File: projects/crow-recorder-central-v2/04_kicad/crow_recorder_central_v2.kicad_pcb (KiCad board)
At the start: 6 copper layers, 170 x 120 mm, 198 parts, among them J1 C381116, J10 C9900035627, J2 C3020560, J3 C9900035627, J4 C9900035627, J5 C9900035627, J6 C9900035627, J7 C9900035627, J8 C9900035627, J9 C9900035627, Q1 C15127, Q2 C20917, U1 C6938291, U10 C6035451, U2 C181312, U3 C181312, U4 C232798, U5 C82317, U6 C2909890, U7 C5224055, U8 C5224055, U9 C150173, Y1 C7190380

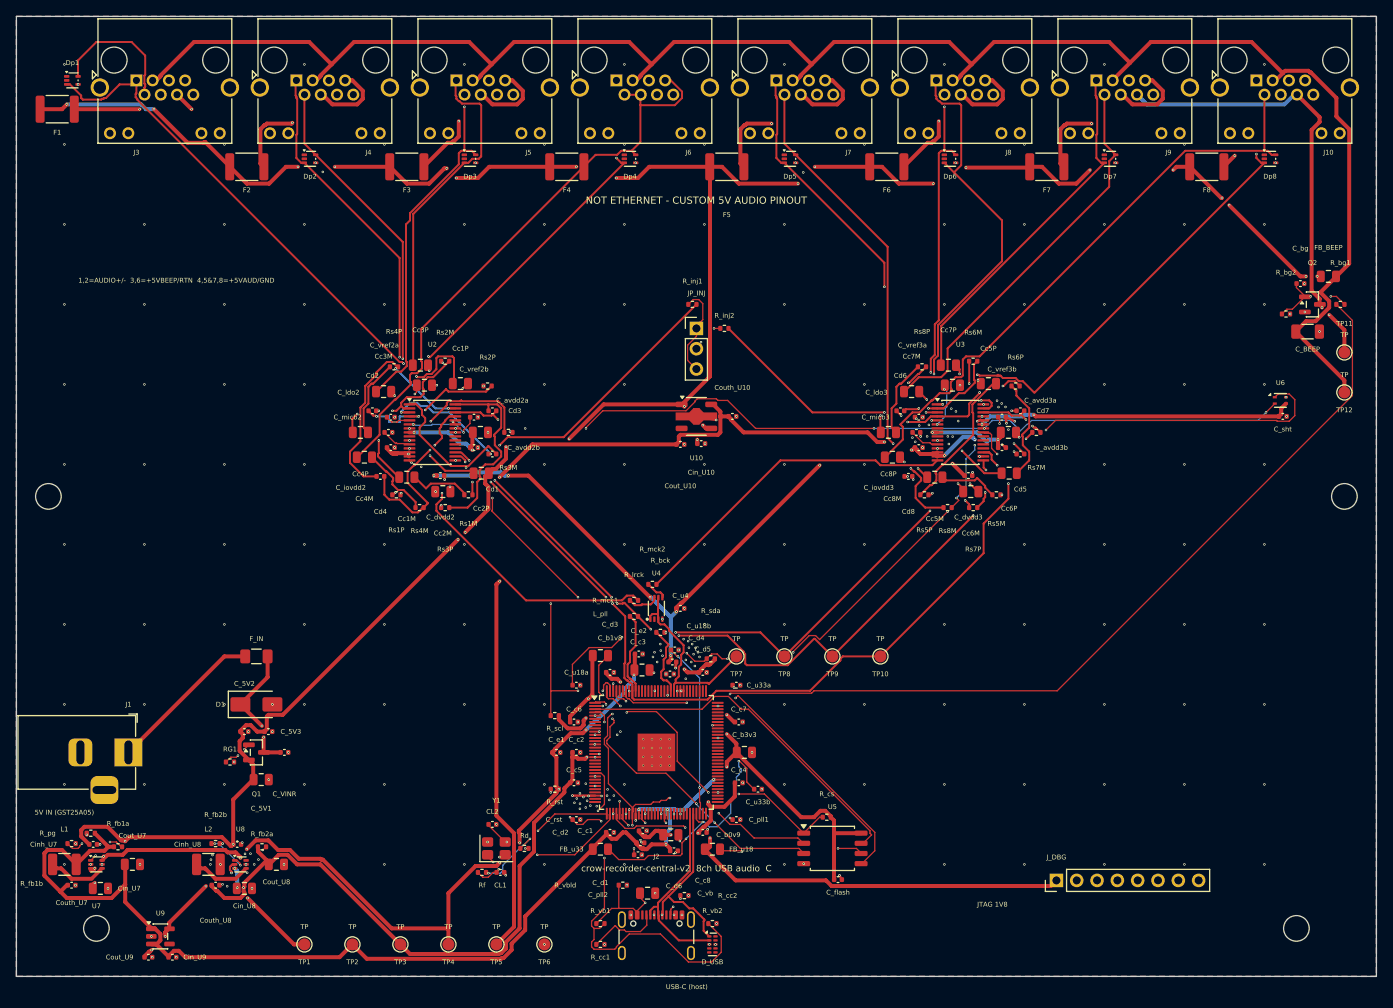
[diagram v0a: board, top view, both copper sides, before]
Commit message: crow-recorder-central-v2 WIP checkpoint: mid-P0 fix pass at the 2026-07-23 quota stop
Session-quota interruption checkpoint. Carries the interrupted P5VA_4
net-merge surgery (schematic doglegs, merged-net tree deletion, port-4 +
channel-2 re-route, 5V island reconnection), check_port_nets.py (the
label-survival gate that found the SECOND merge MID2P->5V the red-team
missed), ADR-0007 PoE-backfeed draft, rebuild_reuse.sh driver, BLM21
part. NOT a green gate — DRC re-verify + scoped re-red-team still owed
(RESUME.md is the brief). GUARD from the red-team dispositions: Q1
reverse-polarity is CORRECT as-built (rejected finding — do not "fix").

Co-Authored-By: Claude Fable 5 <noreply@anthropic.com>
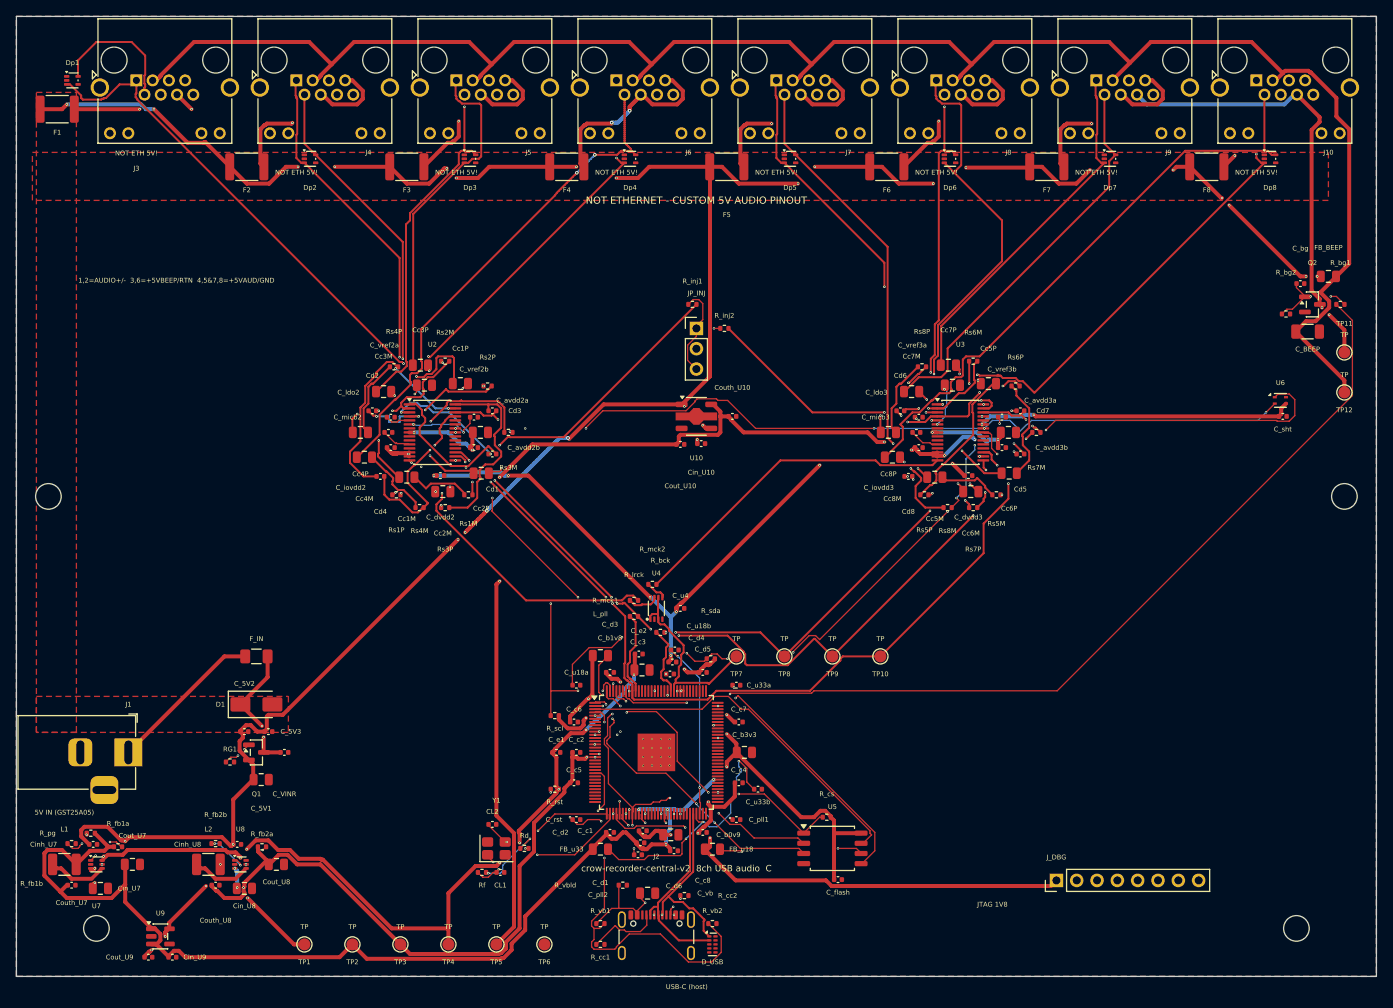
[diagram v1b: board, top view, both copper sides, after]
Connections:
- Cc2P pad 2: 5V -> MID2P
- F4 pad 2: AUDIO4M -> P5VA_4
- J6 pad 4: AUDIO4M -> P5VA_4
- J6 pad 7: AUDIO4M -> P5VA_4
- Rs2P pad 1: 5V -> MID2P
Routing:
- net P5VA_4: track 0.00 -> 24.1 mm, vias 0 -> 2
- net GND: track 21.2 -> 0.00 mm, vias 311 -> 0
- net MID2P: track 0.00 -> 13.3 mm, vias 0 -> 2
- net 5V: track 370.6 -> 358.0 mm, vias 34 -> 33
- net AUDIO4M: track 74.7 -> 63.6 mm, vias 0 -> 2
- added copper zone on F.Cu, net 5V
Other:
- board text added: "NOT ETH 5V!"

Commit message: crow-recorder-central-v2: P0 fix RE-VERIFIED from committed source; P1 set closed; policy_audit 0 FAIL
Resumed from WIP 8017400 (killed mid-rebuild = untrustworthy; re-ran
rebuild_reuse.sh clean). Measured: check_port_nets 115/115 labels + 8/8
ports pin-for-pin; DRC 0/0/0 (--severity-all --refill-zones
--schematic-parity); E-INV 7/7; E-TOPO 2/2; count_parity 194 x4.

route.yaml: unify_zone_priorities dropped from the stitch pass list — the
pass hard-refuses cross-net zone-outline overlap, but the deliberate 5V
patch-pours over the board-wide F.Cu GND pour are priority-resolved and
DRC-gated; usb-hub-3s-v3 sealed with the same pattern and the same pass
absent.

P1 closure (measured evidence in journal + DISPOSITIONS.md): 5V trunk 159
segs all 0.5mm + 1144mm2 pour patches, 6 netclasses in the final
.kicad_pro; P-ADJ over-spans re-measured at their local subjects and
waived with numbers; 8x per-port NOT-ETH silk verified on the board;
ADR-0007 finalized carrying the pod-v2 ADR-0005 USER waiver with an
explicit material-difference check (equal-or-lesser exposure here).

NEW GATE 03_src/audit_board.py (P-POL/P-KEEP): 19 polarity facts + 11
connector keepout checks; red-tested (swapped D1 fact -> FAIL, nonzero).
Waivers: S-OCCL (converter sheet is the machine artifact), P-ADJ (per-net
measurements), R-THERM (U1 EP served by 16 footprint-embedded 0.3mm PTH
thermal pads — checker counts only PCB_VIA objects). 08_reviews/
populated: reconstructed red-team review (verbatim lost to the quota
kill — provenance note in-file) + dispositions ledger.

Co-Authored-By: Claude Fable 5 <noreply@anthropic.com>
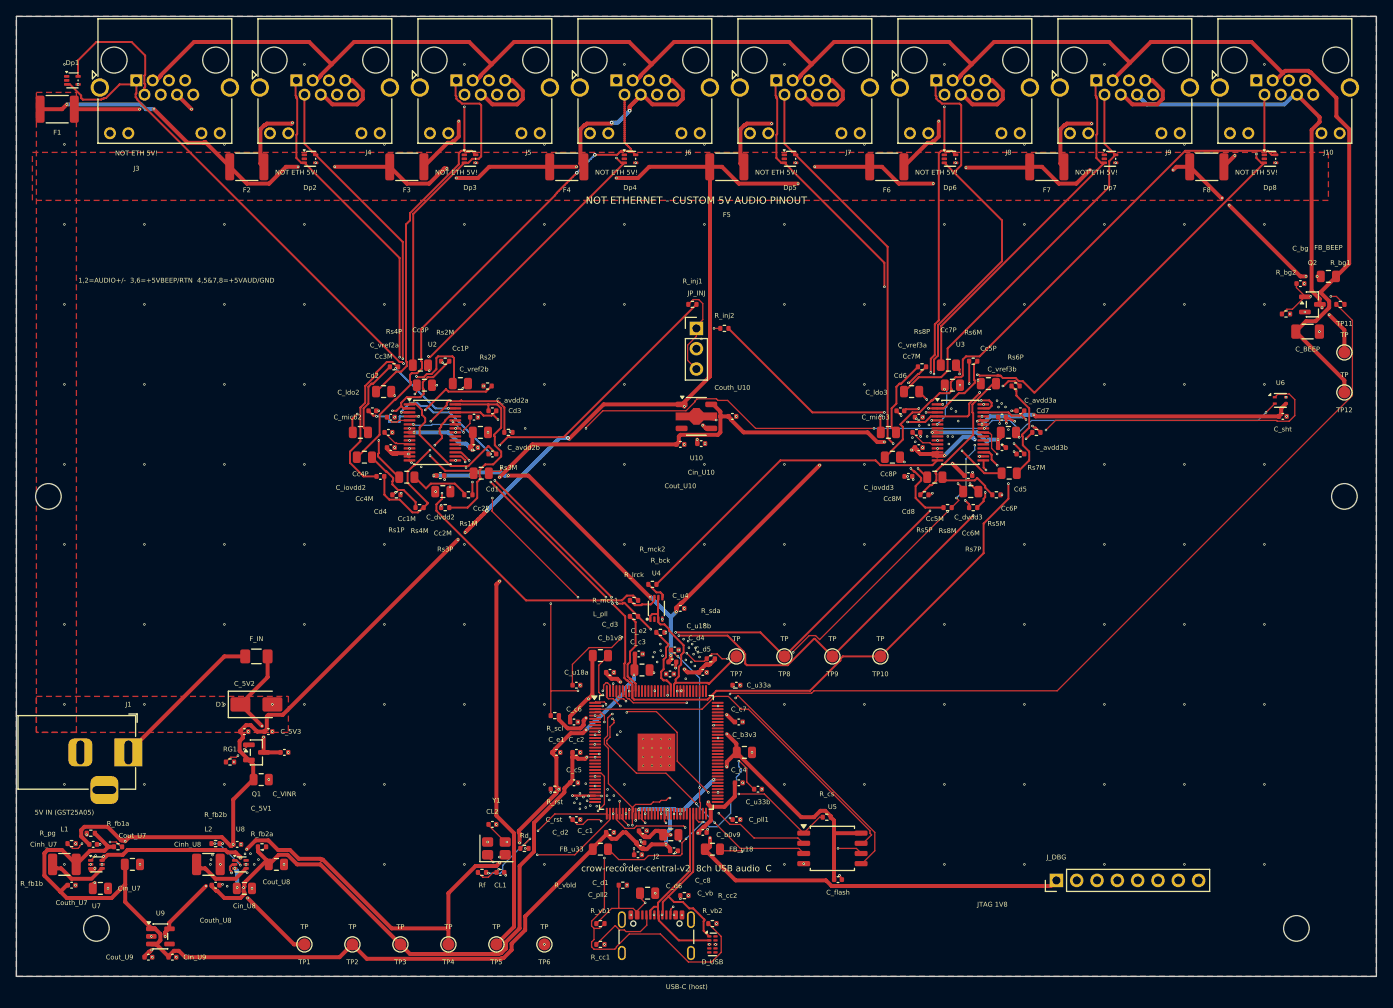
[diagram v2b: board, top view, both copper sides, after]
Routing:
- net GND: track 0.00 -> 21.2 mm, vias 0 -> 307

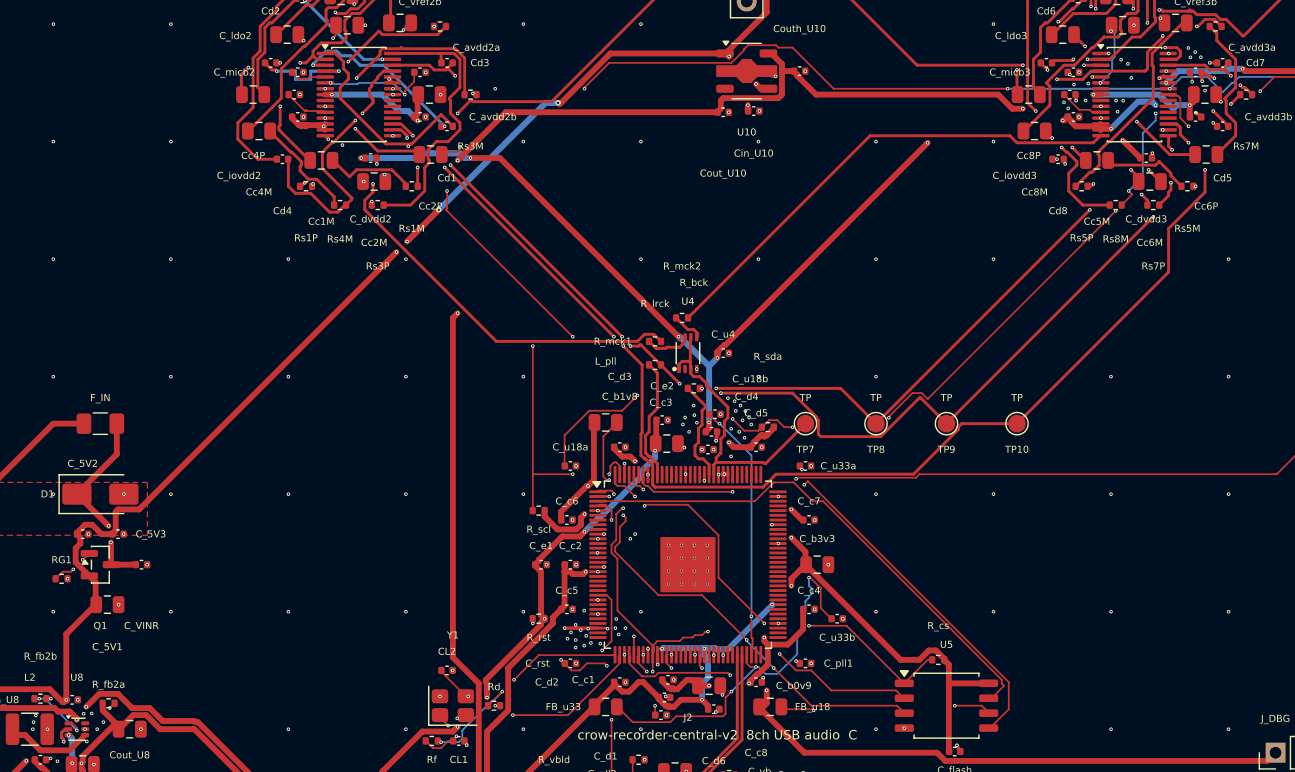
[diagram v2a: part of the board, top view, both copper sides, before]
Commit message: crow-recorder-central-v2 v1.0 source commit S: fresh-lens ORDER, its 2 P1s fixed at source, sourcing staged, twin gate green
Fresh zero-context integrated lens over the staged archive: VERDICT ORDER,
no P0, prior P0s verified repaired (08_reviews/2026-07-23_v1.0_fresh-lens
_integrated.md + DISPOSITIONS FL-*). Its two P1s FIXED pre-seal, not
deferred: CL1/CL2 22pF->12pF C0G C1547 (crystal CL 9pF; eff 14pF was
~30-50ppm of pull) and Cout_U10 1uF->2.2uF 25V X5R C72203 (Torex XC6227
phase-comp; the DETAIL_DESIGN '[PARTS confirm Cout]' placeholder finally
resolved). nets.yaml phantom PLUS5V_AUDIO replaced by the real P5VA_1..8
(measured 0.5mm x120 segments).

Sourcing at SOURCE (tsx supplierPartNumbers; 49-line BOM, every code ==
source): L1/L2 buck inductors (1277AS-H 2R2/1R0, sat-current qualified),
402k E96 for the uncatalogued 400k (-0.17% on 0V9), TLV70018 for
stock-zero TCR2LF18 (ADR-0006 fallback promoted), NX3225SA same-CL-9pF
for the stock-zero FA-238, and the WRONG-PART catch: BLM21PG600SN1D is a
60-ohm bead (Murata code 600 = 60R) — replaced by BLM21SP601SN1D
(600R/2.3A/60mR) in all 4 bead positions before any BOM shipped it.

Twin gate exit 0 (160 OK / 358; 8 evidence-backed adjudications incl. the
C99* consign RJ45 NO-CAD re-proven at 8 fetch attempts and the C464587
alternate-not-a-drop-in probe). CPL 172 (RJ45s + headers excluded,
pod-v2 pattern). Re-gated after every source edit: DRC 0/0/0,
check_port_nets 115/115 + 8/8, E-INV 7/7, count_parity 194x4, audit_board
21+11 (red-tested), policy_audit 0 FAIL exc M-REL (stamps at seal).
Ledgers harvested: proven-parts (beads/inductors/crystal + provenance
updates), lcsc_passives_ledger +8 catalog-verified codes.

Co-Authored-By: Claude Fable 5 <noreply@anthropic.com>
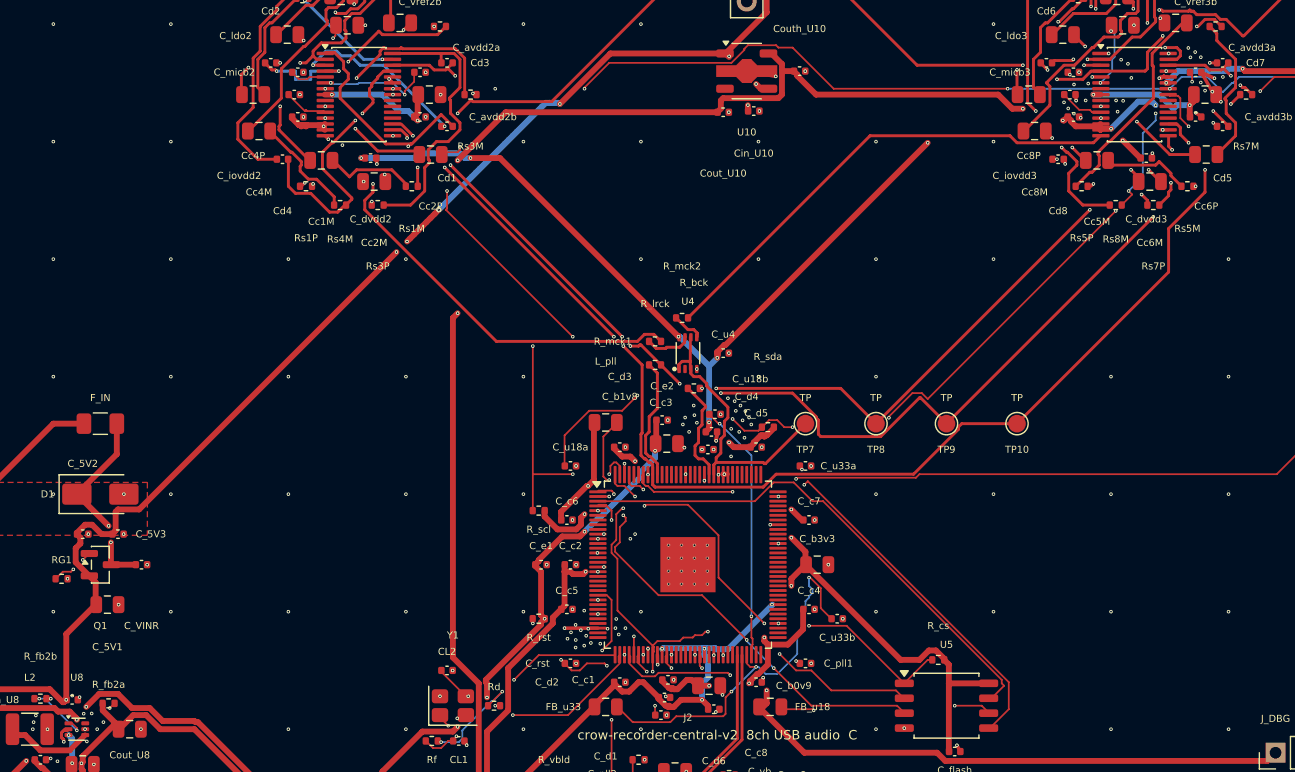
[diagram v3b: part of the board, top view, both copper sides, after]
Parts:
- CL1, CL2: value 22pF -> 12pF
- Cout_U10: value 1uF -> 2.2uF
- R_fb2b: value 400kΩ -> 402kΩ
- U9: value C150173 -> C79924
- Y1: value C7190380 -> C2762192
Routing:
- net GND: track 21.2 -> 22.4 mm, vias 307 -> 311
